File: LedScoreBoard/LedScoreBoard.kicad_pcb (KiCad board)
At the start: 2 copper layers, 149.9 x 149.9 mm, 105 parts, among them J101 LCD, J102 1, J103 10, J104 100, J105 DC12_IN, J106 VDD_IN, J107 PICkit, J108 TweLite-R, Q201 BSS138, Q202 BSS84, Q203 BSS138, Q204 2SJ349, Q205 BSS138, Q206 BSS84, Q207 BSS138, Q208 2SJ349, Q209 BSS138, Q210 BSS84, Q211 BSS138, Q212 2SJ349, Q301 BSS138, Q302 TK40E06N1, Q303 BSS138, Q304 TK40E06N1, Q305 BSS138, Q306 TK40E06N1, Q307 BSS138, Q308 TK40E06N1, Q309 BSS138, Q310 TK40E06N1, Q311 BSS138, Q312 TK40E06N1, Q313 BSS138, Q314 TK40E06N1, SW101 SW_Push, SW102 PlusHun, SW103 MinusHun, SW104 PlusTen, SW105 MinusTen, SW106 PlusOne, SW107 MinusOne, U101 PIC16F1516-ISP, U102 MW-R-WX, U103 LM2931-3.3_TO220, U301 LM358, U302 LM358, U303 LM358, U304 LM358

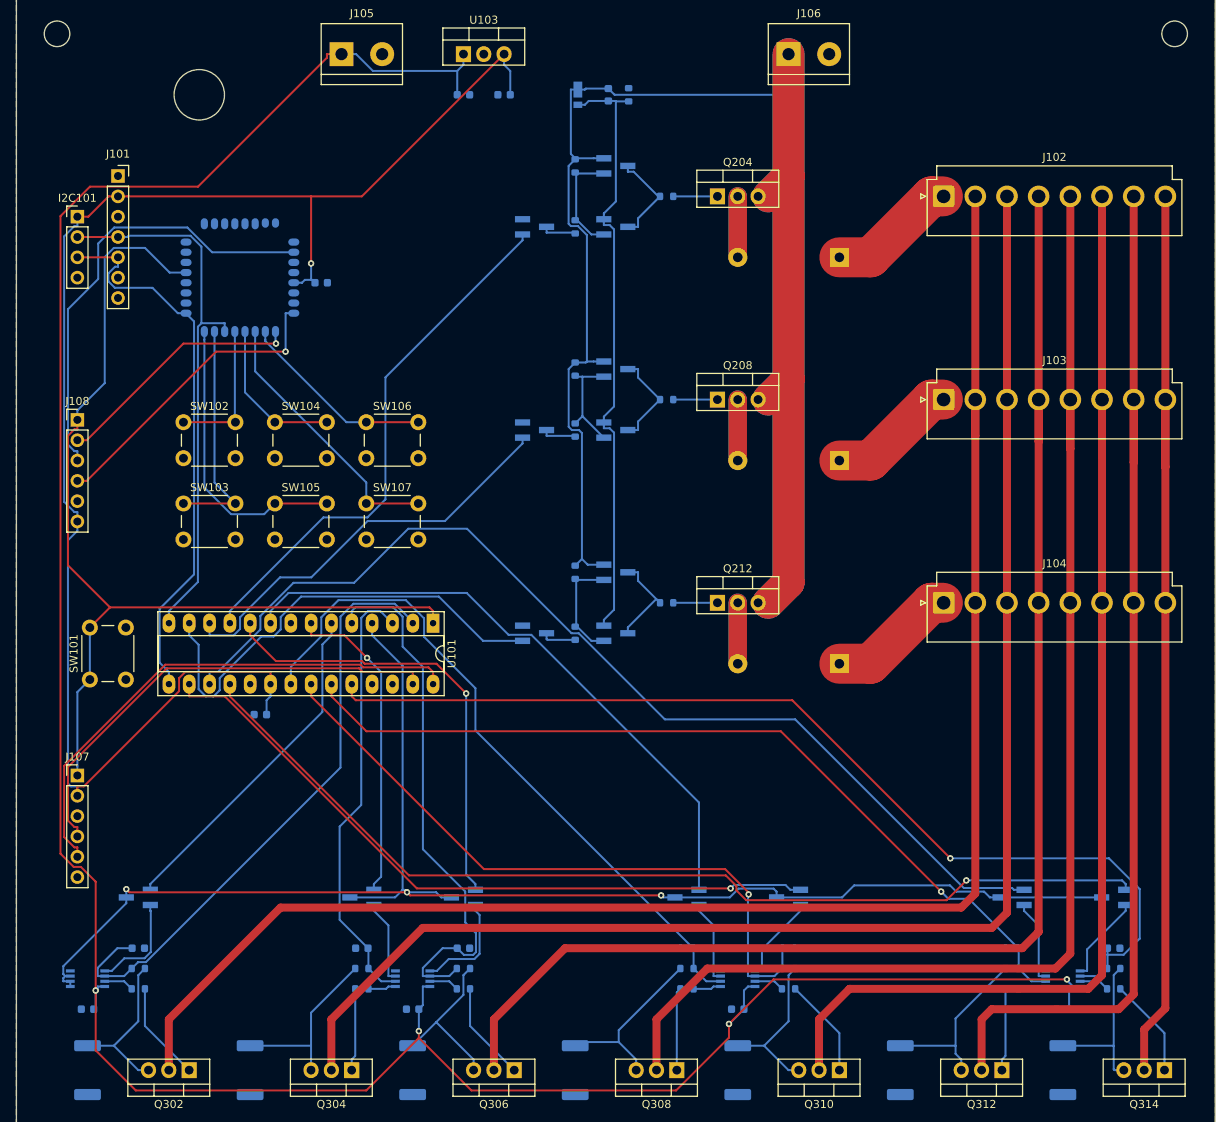
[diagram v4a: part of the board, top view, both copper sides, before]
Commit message: シルク追加
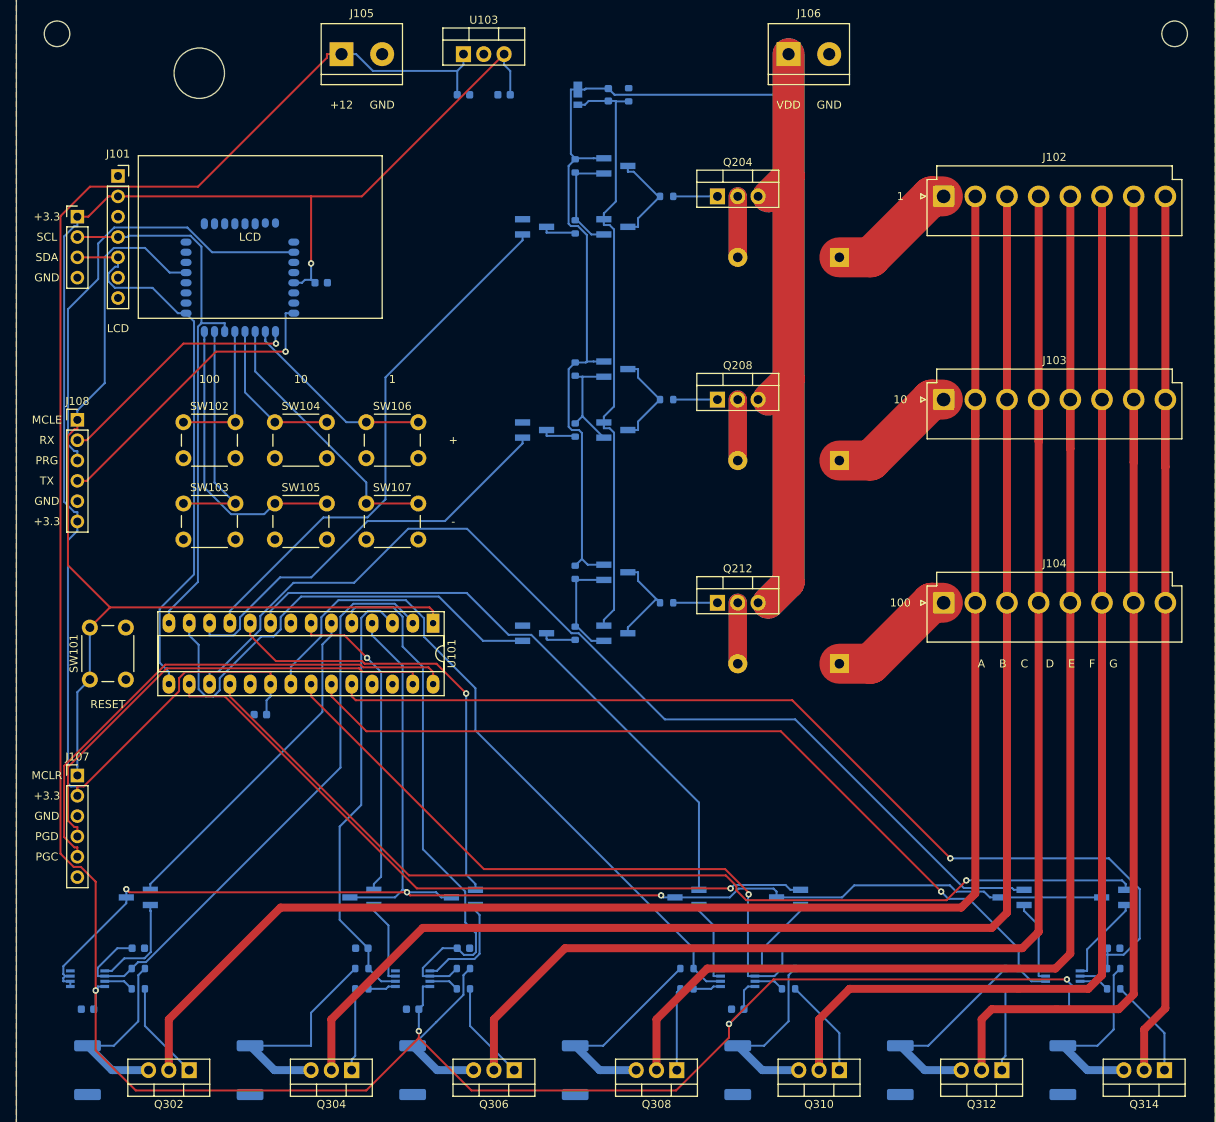
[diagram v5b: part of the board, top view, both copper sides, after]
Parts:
- moved REF05 2.70 mm to (43.2, 35.4)
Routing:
- net Net-(Q304-Pad3): track 22.6 -> 28.4 mm
- net Net-(Q308-Pad3): track 22.4 -> 26.0 mm
- net Net-(Q312-Pad3): track 22.5 -> 26.0 mm
- net Net-(Q314-Pad3): track 20.6 -> 24.0 mm
- net Net-(Q310-Pad3): track 20.1 -> 23.4 mm
- net Net-(Q302-Pad3): track 20.1 -> 23.4 mm
- net Net-(Q306-Pad3): track 20.6 -> 21.5 mm
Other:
- board text added: "+"
- board text added: "+12"
- board text added: "+3.3"
- board text added: "-"
- board text added: "1"
- board text added: "10"
- board text added: "100"
- board text added: "A B C D E F G"
- board text added: "GND"
- board text added: "LCD"
- board text added: "MCLE"
- board text added: "MCLR"
- board text added: "PGC"
- board text added: "PGD"
- board text added: "PRG"
- board text added: "RESET"
- board text added: "RX"
- board text added: "SCL"
- board text added: "SDA"
- board text added: "TX"
- board text added: "VDD"

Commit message: ヒートシンク穴追加
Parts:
- added REF06: MountingHole_2.2mm_M2, MountingHole:MountingHole_2.2mm_M2, F.Cu at (110.5, 44.5)
- added REF07: MountingHole_2.2mm_M2, MountingHole:MountingHole_2.2mm_M2, F.Cu at (110.5, 69.8)
- added REF08: MountingHole_2.2mm_M2, MountingHole:MountingHole_2.2mm_M2, F.Cu at (110.5, 95.2)
- added REF09: MountingHole_2.2mm_M2, MountingHole:MountingHole_2.2mm_M2, F.Cu at (39.4, 166.4)
- added REF10: MountingHole_2.2mm_M2, MountingHole:MountingHole_2.2mm_M2, F.Cu at (59.7, 166.4)
- added REF11: MountingHole_2.2mm_M2, MountingHole:MountingHole_2.2mm_M2, F.Cu at (80.0, 166.4)
- added REF12: MountingHole_2.2mm_M2, MountingHole:MountingHole_2.2mm_M2, F.Cu at (100.3, 166.4)
- added REF13: MountingHole_2.2mm_M2, MountingHole:MountingHole_2.2mm_M2, F.Cu at (120.7, 166.4)
- added REF14: MountingHole_2.2mm_M2, MountingHole:MountingHole_2.2mm_M2, F.Cu at (141.0, 166.4)
- added REF15: MountingHole_2.2mm_M2, MountingHole:MountingHole_2.2mm_M2, F.Cu at (161.3, 166.4)
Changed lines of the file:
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@@
     )
+  )
+  (footprint "MountingHole:MountingHole_2.2mm_M2" locked (layer "F.Cu")
+    (at 110.49 69.85)
+    (descr "Mounting Hole 2.2mm, no annular, M2")
+    (tags "mounting hole 2.2mm no annular m2")
+    (attr exclude_from_pos_files exclude_from_bom)
+    (fp_text reference "REF07" (at 0 -3.2) (layer "F.SilkS") hide
+      (effects (font (size 1 1) (thickness 0.15)))
+    )
+    (fp_text value "MountingHole_2.2mm_M2" (at 0 3.2) (layer "F.Fab")
+      (effects (font (size 1 1) (thickness 0.15)))
+    )
+    (fp_text user "${REFERENCE}" (at 0 0) (layer "F.Fab")
+      (effects (font (size 1 1) (thickness 0.15)))
+    )
+    (fp_circle (center 0 0) (end 2.2 0) (layer "Cmts.User") (width 0.15) (fill none))
+    (fp_circle (center 0 0) (end 2.45 0) (layer "F.CrtYd") (width 0.05) (fill none))
+    (pad "" np_thru_hole circle locked (at 0 0) (size 2.2 2.2) (drill 2.2) (layers *.Cu *.Mask))
   )
   (footprint "MountingHole:MountingHole_3.2mm_M3" locked (layer "F.Cu")
@@
     )
   )
+  (footprint "MountingHole:MountingHole_2.2mm_M2" locked (layer "F.Cu")
+    (at 110.49 95.25)
+    (descr "Mounting Hole 2.2mm, no annular, M2")
+    (tags "mounting hole 2.2mm no annular m2")
+    (attr exclude_from_pos_files exclude_from_bom)
+    (fp_text reference "REF08" (at 0 -3.2) (layer "F.SilkS") hide
+      (effects (font (size 1 1) (thickness 0.15)))
+    )
+    (fp_text value "MountingHole_2.2mm_M2" (at 0 3.2) (layer "F.Fab")
+      (effects (font (size 1 1) (thickness 0.15)))
+    )
+    (fp_text user "${REFERENCE}" (at 0 0) (layer "F.Fab")
+      (effects (font (size 1 1) (thickness 0.15)))
+    )
+    (fp_circle (center 0 0) (end 2.2 0) (layer "Cmts.User") (width 0.15) (fill none))
+    (fp_circle (center 0 0) (end 2.45 0) (layer "F.CrtYd") (width 0.05) (fill none))
+    (pad "" np_thru_hole circle locked (at 0 0) (size 2.2 2.2) (drill 2.2) (layers *.Cu *.Mask))
+  )
   (footprint "Connector_PinHeader_2.54mm:PinHeader_1x06_P2.54mm_Vertical" (layer "F.Cu")
     (at 27.94 123.19)
@@
     (pad "" np_thru_hole circle locked (at 0 0) (size 3.2 3.2) (drill 3.2) (layers *.Cu *.Mask))
   )
+  (footprint "MountingHole:MountingHole_2.2mm_M2" locked (layer "F.Cu")
+    (at 39.37 166.37)
+    (descr "Mounting Hole 2.2mm, no annular, M2")
+    (tags "mounting hole 2.2mm no annular m2")
+    (attr exclude_from_pos_files exclude_from_bom)
+    (fp_text reference "REF09" (at 0 -3.2) (layer "F.SilkS") hide
+      (effects (font (size 1 1) (thickness 0.15)))
+    )
+    (fp_text value "MountingHole_2.2mm_M2" (at 0 3.2) (layer "F.Fab")
+      (effects (font (size 1 1) (thickness 0.15)))
+    )
+    (fp_text user "${REFERENCE}" (at 0 0) (layer "F.Fab")
+      (effects (font (size 1 1) (thickness 0.15)))
+    )
+    (fp_circle (center 0 0) (end 2.2 0) (layer "Cmts.User") (width 0.15) (fill none))
+    (fp_circle (center 0 0) (end 2.45 0) (layer "F.CrtYd") (width 0.05) (fill none))
+    (pad "" np_thru_hole circle locked (at 0 0) (size 2.2 2.2) (drill 2.2) (layers *.Cu *.Mask))
+  )
+  (footprint "MountingHole:MountingHole_2.2mm_M2" locked (layer "F.Cu")
+    (at 59.69 166.37)
+    (descr "Mounting Hole 2.2mm, no annular, M2")
+    (tags "mounting hole 2.2mm no annular m2")
+    (attr exclude_from_pos_files exclude_from_bom)
+    (fp_text reference "REF10" (at 0 -3.2) (layer "F.SilkS") hide
+      (effects (font (size 1 1) (thickness 0.15)))
+    )
+    (fp_text value "MountingHole_2.2mm_M2" (at 0 3.2) (layer "F.Fab")
+      (effects (font (size 1 1) (thickness 0.15)))
+    )
+    (fp_text user "${REFERENCE}" (at 0 0) (layer "F.Fab")
+      (effects (font (size 1 1) (thickness 0.15)))
+    )
+    (fp_circle (center 0 0) (end 2.2 0) (layer "Cmts.User") (width 0.15) (fill none))
+    (fp_circle (center 0 0) (end 2.45 0) (layer "F.CrtYd") (width 0.05) (fill none))
+    (pad "" np_thru_hole circle locked (at 0 0) (size 2.2 2.2) (drill 2.2) (layers *.Cu *.Mask))
+  )
   (footprint "Package_TO_SOT_THT:TO-220-3_Vertical" (layer "F.Cu")
     (at 107.95 101.6)
@@
       (rotate (xyz 0 0 0))
     )
+  )
+  (footprint "MountingHole:MountingHole_2.2mm_M2" locked (layer "F.Cu")
+    (at 140.97 166.37)
+    (descr "Mounting Hole 2.2mm, no annular, M2")
+    (tags "mounting hole 2.2mm no annular m2")
+    (attr exclude_from_pos_files exclude_from_bom)
+    (fp_text reference "REF14" (at 0 -3.2) (layer "F.SilkS") hide
+      (effects (font (size 1 1) (thickness 0.15)))
+    )
+    (fp_text value "MountingHole_2.2mm_M2" (at 0 3.2) (layer "F.Fab")
+      (effects (font (size 1 1) (thickness 0.15)))
+    )
+    (fp_text user "${REFERENCE}" (at 0 0) (layer "F.Fab")
+      (effects (font (size 1 1) (thickness 0.15)))
+    )
+    (fp_circle (center 0 0) (end 2.2 0) (layer "Cmts.User") (width 0.15) (fill none))
+    (fp_circle (center 0 0) (end 2.45 0) (layer "F.CrtYd") (width 0.05) (fill none))
+    (pad "" np_thru_hole circle locked (at 0 0) (size 2.2 2.2) (drill 2.2) (layers *.Cu *.Mask))
   )
   (footprint "Package_TO_SOT_THT:TO-220-3_Vertical" (layer "F.Cu")
@@
       (rotate (xyz 0 0 0))
     )
+  )
+  (footprint "MountingHole:MountingHole_2.2mm_M2" locked (layer "F.Cu")
+    (at 100.33 166.37)
+    (descr "Mounting Hole 2.2mm, no annular, M2")
+    (tags "mounting hole 2.2mm no annular m2")
+    (attr exclude_from_pos_files exclude_from_bom)
+    (fp_text reference "REF12" (at 0 -3.2) (layer "F.SilkS") hide
+      (effects (font (size 1 1) (thickness 0.15)))
+    )
+    (fp_text value "MountingHole_2.2mm_M2" (at 0 3.2) (layer "F.Fab")
+      (effects (font (size 1 1) (thickness 0.15)))
+    )
+    (fp_text user "${REFERENCE}" (at 0 0) (layer "F.Fab")
+      (effects (font (size 1 1) (thickness 0.15)))
+    )
+    (fp_circle (center 0 0) (end 2.2 0) (layer "Cmts.User") (width 0.15) (fill none))
+    (fp_circle (center 0 0) (end 2.45 0) (layer "F.CrtYd") (width 0.05) (fill none))
+    (pad "" np_thru_hole circle locked (at 0 0) (size 2.2 2.2) (drill 2.2) (layers *.Cu *.Mask))
+  )
+  (footprint "MountingHole:MountingHole_2.2mm_M2" locked (layer "F.Cu")
+    (at 80.01 166.37)
+    (descr "Mounting Hole 2.2mm, no annular, M2")
+    (tags "mounting hole 2.2mm no annular m2")
+    (attr exclude_from_pos_files exclude_from_bom)
+    (fp_text reference "REF11" (at 0 -3.2) (layer "F.SilkS") hide
+      (effects (font (size 1 1) (thickness 0.15)))
+    )
+    (fp_text value "MountingHole_2.2mm_M2" (at 0 3.2) (layer "F.Fab")
+      (effects (font (size 1 1) (thickness 0.15)))
+    )
+    (fp_text user "${REFERENCE}" (at 0 0) (layer "F.Fab")
+      (effects (font (size 1 1) (thickness 0.15)))
+    )
+    (fp_circle (center 0 0) (end 2.2 0) (layer "Cmts.User") (width 0.15) (fill none))
+    (fp_circle (center 0 0) (end 2.45 0) (layer "F.CrtYd") (width 0.05) (fill none))
+    (pad "" np_thru_hole circle locked (at 0 0) (size 2.2 2.2) (drill 2.2) (layers *.Cu *.Mask))
   )
   (footprint "Package_TO_SOT_THT:TO-220-3_Vertical" (layer "F.Cu")
@@
     )
   )
+  (footprint "MountingHole:MountingHole_2.2mm_M2" locked (layer "F.Cu")
+    (at 110.49 44.45)
+    (descr "Mounting Hole 2.2mm, no annular, M2")
+    (tags "mounting hole 2.2mm no annular m2")
+    (attr exclude_from_pos_files exclude_from_bom)
+    (fp_text reference "REF06" (at 0 -3.2) (layer "F.SilkS") hide
+      (effects (font (size 1 1) (thickness 0.15)))
+    )
+    (fp_text value "MountingHole_2.2mm_M2" (at 0 3.2) (layer "F.Fab")
+      (effects (font (size 1 1) (thickness 0.15)))
+    )
+    (fp_text user "${REFERENCE}" (at 0 0) (layer "F.Fab")
+      (effects (font (size 1 1) (thickness 0.15)))
+    )
+    (fp_circle (center 0 0) (end 2.2 0) (layer "Cmts.User") (width 0.15) (fill none))
+    (fp_circle (center 0 0) (end 2.45 0) (layer "F.CrtYd") (width 0.05) (fill none))
+    (pad "" np_thru_hole circle locked (at 0 0) (size 2.2 2.2) (drill 2.2) (layers *.Cu *.Mask))
+  )
   (footprint "Button_Switch_THT:SW_PUSH_6mm" (layer "F.Cu")
     (at 64.06 79.03)
@@
     )
   )
+  (footprint "MountingHole:MountingHole_2.2mm_M2" locked (layer "F.Cu")
+    (at 120.65 166.37)
+    (descr "Mounting Hole 2.2mm, no annular, M2")
+    (tags "mounting hole 2.2mm no annular m2")
+    (attr exclude_from_pos_files exclude_from_bom)
+    (fp_text reference "REF13" (at 0 -3.2) (layer "F.SilkS") hide
+      (effects (font (size 1 1) (thickness 0.15)))
+    )
+    (fp_text value "MountingHole_2.2mm_M2" (at 0 3.2) (layer "F.Fab")
+      (effects (font (size 1 1) (thickness 0.15)))
+    )
+    (fp_text user "${REFERENCE}" (at 0 0) (layer "F.Fab")
+      (effects (font (size 1 1) (thickness 0.15)))
+    )
+    (fp_circle (center 0 0) (end 2.2 0) (layer "Cmts.User") (width 0.15) (fill none))
+    (fp_circle (center 0 0) (end 2.45 0) (layer "F.CrtYd") (width 0.05) (fill none))
+    (pad "" np_thru_hole circle locked (at 0 0) (size 2.2 2.2) (drill 2.2) (layers *.Cu *.Mask))
+  )
   (footprint "Connector_PinHeader_2.54mm:PinHeader_1x04_P2.54mm_Vertical" (layer "F.Cu")
     (at 27.94 53.34)
@@
     )
   )
+  (footprint "MountingHole:MountingHole_2.2mm_M2" locked (layer "F.Cu")
+    (at 161.29 166.37)
+    (descr "Mounting Hole 2.2mm, no annular, M2")
+    (tags "mounting hole 2.2mm no annular m2")
+    (attr exclude_from_pos_files exclude_from_bom)
+    (fp_text reference "REF15" (at 0 -3.2) (layer "F.SilkS") hide
+      (effects (font (size 1 1) (thickness 0.15)))
+    )
+    (fp_text value "MountingHole_2.2mm_M2" (at 0 3.2) (layer "F.Fab")
+      (effects (font (size 1 1) (thickness 0.15)))
+    )
+    (fp_text user "${REFERENCE}" (at 0 0) (layer "F.Fab")
+      (effects (font (size 1 1) (thickness 0.15)))
+    )
+    (fp_circle (center 0 0) (end 2.2 0) (layer "Cmts.User") (width 0.15) (fill none))
+    (fp_circle (center 0 0) (end 2.45 0) (layer "F.CrtYd") (width 0.05) (fill none))
+    (pad "" np_thru_hole circle locked (at 0 0) (size 2.2 2.2) (drill 2.2) (layers *.Cu *.Mask))
+  )
   (footprint "Package_TO_SOT_THT:TO-220-3_Vertical" (layer "F.Cu")
